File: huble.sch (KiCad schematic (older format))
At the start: 32 parts, among them J7 USB_C_Receptacle, J8 USB_C_Receptacle, P1 CONN_01X04, P2 CONN_02X03, Q1 Q_PMOS_GSD, Q2 Q_PMOS_GSD, U3 rgbled, U4 ATmega32U4, U5 24LC16, Y2 Crystal_GND24

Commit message: fixed missing cap on schematic, and fixed up post move netlist
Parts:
- C9: footprint Capacitors_Tantalum_SMD:TantalC_SizeA_EIA-3216_Wave -> Capacitors_Tantalum_SMD:CP_Tantalum_Case-A_EIA-3216-18_Reflow
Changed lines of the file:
@@
 $Descr A4 11693 8268
 encoding utf-8
-Sheet 2 3
+Sheet 2 2
 Title "Huble"
 Date "2017-08-16"
@@
 F 0 "C9" H 5768 1346 50  0000 L CNN
 F 1 "47u 6.3v" H 5768 1255 50  0000 L CNN
-F 2 "Capacitors_Tantalum_SMD:TantalC_SizeA_EIA-3216_Wave" H 5688 1150 50  0001 C CNN
+F 2 "Capacitors_Tantalum_SMD:CP_Tantalum_Case-A_EIA-3216-18_Reflow" H 5688 1150 50  0001 C CNN
 F 3 "" H 5650 1300 50  0000 C CNN
 F 4 "1432351" H 5650 1300 60  0001 C CNN "farnell #"
@@
 $EndComp
 $Comp
-L +5C #PWR?
+L +5C #PWR053
 U 1 1 5A6A530B
 P 2050 750
-F 0 "#PWR?" H 2050 600 50  0001 C CNN
+F 0 "#PWR053" H 2050 600 50  0001 C CNN
 F 1 "+5C" H 2065 923 50  0000 C CNN
 F 2 "" H 2050 750 50  0001 C CNN
@@
 $EndComp
 $Comp
-L +5C #PWR?
+L +5C #PWR054
 U 1 1 5A6A53AB
 P 2150 4200
-F 0 "#PWR?" H 2150 4050 50  0001 C CNN
+F 0 "#PWR054" H 2150 4050 50  0001 C CNN
 F 1 "+5C" H 2165 4373 50  0000 C CNN
 F 2 "" H 2150 4200 50  0001 C CNN

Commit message: remove wrong farnell codes, use same 47u tant cap in both places
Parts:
- J7, J8: farnell # 2564554 -> 2524075
- R14, R15, R16: farnell # 2447609 -> (none)
- Y2: value Crystal_GND24 -> 16mhz
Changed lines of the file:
@@
 F 2 "Resistors_SMD:R_0805" V 8480 5400 30  0001 C CNN
 F 3 "" H 8550 5400 30  0000 C CNN
-F 4 "2447609" H 8550 5400 60  0001 C CNN "farnell #"
 	1    8550 5400
 	0    1    1    0
@@
 F 2 "Resistors_SMD:R_0805" V 8480 5700 30  0001 C CNN
 F 3 "" H 8550 5700 30  0000 C CNN
-F 4 "2447609" H 8550 5700 60  0001 C CNN "farnell #"
 	1    8550 5700
 	0    1    1    0
@@
 F 2 "Resistors_SMD:R_0805" V 8480 6000 30  0001 C CNN
 F 3 "" H 8550 6000 30  0000 C CNN
-F 4 "2447609" H 8550 6000 60  0001 C CNN "farnell #"
 	1    8550 6000
 	0    1    1    0
@@
 F 2 "fp:usb-c-24smt" H 1350 2350 50  0001 C CNN
 F 3 "http://www.usb.org/developers/docs/usb_31_033017.zip" H 1350 2350 50  0001 C CNN
-F 4 "2564554" H 1200 2350 60  0001 C CNN "farnell #"
+F 4 "2524075" H 1200 2350 60  0001 C CNN "farnell #"
 	1    1200 2350
 	1    0    0    -1
@@
 P 7300 3800
 F 0 "Y2" V 7254 4041 50  0000 L CNN
-F 1 "Crystal_GND24" V 7345 4041 50  0000 L CNN
+F 1 "16mhz" V 7345 4041 50  0000 L CNN
 F 2 "Crystals:Crystal_SMD_3225-4pin_3.2x2.5mm" H 7300 3800 50  0001 C CNN
 F 3 "" H 7300 3800 50  0001 C CNN
@@
 F 2 "fp:usb-c-24smt" H 1400 5750 50  0001 C CNN
 F 3 "http://www.usb.org/developers/docs/usb_31_033017.zip" H 1400 5750 50  0001 C CNN
-F 4 "2564554" H 1250 5750 60  0001 C CNN "farnell #"
+F 4 "2524075" H 1250 5750 60  0001 C CNN "farnell #"
 	1    1250 5750
 	1    0    0    -1

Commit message: updated for BOM
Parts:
- removed C12, C13: 20pf, Capacitors_SMD:C_0805, symbol C
- removed U5: 24LC16, Housings_SOIC:SOIC-8_3.9x4.9mm_Pitch1.27mm, symbol 24LC16
- removed Y2: 16mhz, Crystals:Crystal_SMD_3225-4pin_3.2x2.5mm, symbol Crystal_GND24
- added R20, R22, R23: 60R, 125mW, 5%, Resistors_SMD:R_0805, symbol R
- added R21: 100R, 125mW, 5%, Resistors_SMD:R_0805, symbol R
- added U5, U6: 4 pin RGB led, com anode, red: 500mcd 620nm. Gree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, fp:3528-4p, symbol rgbled
- C10: value 4.7u -> 4.7uF, ceramic, 6v, 10%, x5r; supplier (none) -> any/open
- C11: value 0.1u -> 0.1uF, ceramic, 6v, 10%, x5r; supplier (none) -> any/open
- C14: value 1u -> 1uF, ceramic, 6v, 10%, x5r; supplier (none) -> any/open
- C9: value 47u 6.3v -> 47uF, 6.3v, 10%, tantalum; supplier (none) -> AVX; supplier PN (none) -> TAJC476K006RNJ
- J7, J8: value USB_C_Receptacle -> USB C type 2.0 SMT 16pin; farnell # 2524075 -> (none); supplier (none) -> contact technology corp; supplier PN (none) -> sbc-160s-202-s338
- P1, P2, TP11, TP3, W1, W2: supplier (none) -> dnp
- Q1, Q2: value Q_PMOS_GSD -> PMOS, -3.6A, 0.02R; supplier (none) -> diodes inc; supplier PN (none) -> DMP2035U
- R10, R9: value 4.7k -> 4.7k, 125mW, 5%; supplier (none) -> any/open
- R11: value 10k -> 10k, 125mW, 5%; farnell # 2447553 -> (none); supplier (none) -> any/open
- R12: value 22r -> 100R, 125mW, 5%; farnell # 2447609 -> (none); supplier (none) -> any/open
- R13: value 22r -> 60R, 125mW, 5%; farnell # 2447609 -> (none); supplier (none) -> any/open
- R14: value 100R -> 100R, 125mW, 5%; supplier (none) -> any/open
- R15, R16: value 60R -> 60R, 125mW, 5%; supplier (none) -> any/open
- R18, R19: value 10k -> 10k, 125mW, 5%; farnell # 2073784 -> (none); supplier (none) -> any/open
- R7, R8: farnell # 9333681 -> (none); supplier (none) -> dnp
- U3: value rgbled -> 4 pin RGB led, com anode, red: 500mcd 620nm. Green: 1000mcd 520nm. Blue: 500mcd 460nm.; supplier (none) -> any/open
- U4: value ATmega32U4 -> atmel samd21g; farnell # 2425127 -> (none); supplier (none) -> microchip; supplier PN (none) -> ATSAMD21G18A-MU
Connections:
- wire segments 54 -> 49
- no-connect marks 41 -> 40
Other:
- note added: "can't use the same power flag on both lines, or they get connected together!"
- note added: "will need level conversion if switching to 3.3v arm"
- note removed: "1579573"
- note removed: "256kbit eeprom for extra layers"
- note removed: "load cap is 20pf. assume stray cap is 5pf, so use 30pf caps"

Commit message: v2.1 ready for fab
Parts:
- removed C9: 47uF, 6.3v, 10%, tantalum, Capacitors_Tantalum_SMD:CP_Tantalum_Case-A_EIA-3216-18_Reflow, symbol CP
- removed J7, J8: USB C type 2.0 SMT 16pin, fp:usb-c-24smt, symbol USB_C_Receptacle
- removed P1: CONN_01X04, Pin_Headers:Pin_Header_Straight_1x04_Pitch2.54mm, symbol Conn_01x04
- removed Q1, Q2: PMOS, -3.6A, 0.02R, TO_SOT_Packages_SMD:SOT-23, symbol Q_PMOS_GSD
- removed R11, R18, R19: 10k, 125mW, 5%, Resistors_SMD:R_0805, symbol R
- removed TP11: TEST, Measurement_Points:Measurement_Point_Round-SMD-Pad_Small, symbol TEST
- removed U4: atmel samd21g, Housings_DFN_QFN:QFN-44-1EP_7x7mm_Pitch0.5mm, symbol ATmega32U4-RESCUE-huble
- removed W1, W2: TEST_1P, Measurement_Points:Measurement_Point_Round-SMD-Pad_Small, symbol TEST_1P
- added C12, C13, C9: 0.1uF, ceramic, 6v, 10%, x5r, Capacitors_SMD:C_0603, symbol C
- added C16: 20pf, ceramic, 6v, 5%, Capacitors_SMD:C_0603, symbol C
- added J2, J3: USB_C_Receptacle_16pin, fp:usb-c-16smt, symbol USB_C_Receptacle_16pin
- added Q1, Q2, Q3, Q4: Q_NMOS_GSD, TO_SOT_Packages_SMD:SOT-323_SC-70, symbol Q_NMOS_GSD
- added TP1, TP2, TP4: TEST, Measurement_Points:Measurement_Point_Round-SMD-Pad_Small, symbol TEST
- added U4: samd21j, Housings_DFN_QFN:QFN-64-1EP_9x9mm_Pitch0.5mm, symbol samd21j
- added U7: MMBZx, TO_SOT_Packages_SMD:SOT-23, symbol MMBZx
- added Y2: 32.768khz, Crystals:Crystal_SMD_3215-2pin_3.2x1.5mm, symbol Crystal
- C10: value 4.7uF, ceramic, 6v, 10%, x5r -> 10uF, ceramic, 6v, 10%, x5r; footprint Capacitors_SMD:C_0805 -> Capacitors_SMD:C_0603; MOQ (none) -> Value; leadtime (none) -> Value; supplier PN (none) -> Value
- C11: footprint Capacitors_SMD:C_0805 -> Capacitors_SMD:C_0603; MOQ (none) -> Value; leadtime (none) -> Value; supplier PN (none) -> Value
- C14: value 1uF, ceramic, 6v, 10%, x5r -> 20pf, ceramic, 6v, 5%; footprint Capacitors_SMD:C_0805 -> Capacitors_SMD:C_0603; farnell # 1759422 -> 2581087
- R10, R9: value 4.7k, 125mW, 5% -> 10k, 125mW, 5%; footprint Resistors_SMD:R_0805 -> Resistors_SMD:R_0603
- R12, R13, R14, R15, R16, R20, R21, R22, R23: footprint Resistors_SMD:R_0805 -> Resistors_SMD:R_0603
- R7, R8: value 0R -> 10k, 125mW, 5%; footprint Resistors_SMD:R_0805 -> Resistors_SMD:R_0603; farnell # (none) -> 2073784; supplier dnp -> any/open
- TP3: supplier dnp -> (none)
- U3, U5, U6: MOQ (none) -> Value; leadtime (none) -> Value; supplier PN (none) -> Value
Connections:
- net labels added: +3.3V, dfp-l-cc, dfp-r-cc, gclk_io_0, left-usb-gnd, pwm1_b, pwm1_g, pwm1_r, pwm2_b, pwm2_g, pwm2_r, pwm3_b, pwm3_g, pwm3_r, right-usb-gnd, scl5, sda5, swclk, swdio, ufp-cc
- net labels removed: +5C, miso, mosi, pwm_b, pwm_g, pwm_r, sck, usbc-dn, usbc-dp
- wire segments 49 -> 53
- no-connect marks 40 -> 32
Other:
- note added: "esd protection"
- note added: "https://www.nxp.com/docs/en/application-note/AN10441.pdf"
- note added: "level translate\n"
- note removed: "can't use the same power flag on both lines, or they get connected together!"
- note removed: "will need level conversion if switching to 3.3v arm"
- moved on the sheet: P2, R10, R12, R13, R14, R15, R16, R20, R21, R22, R23, R9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

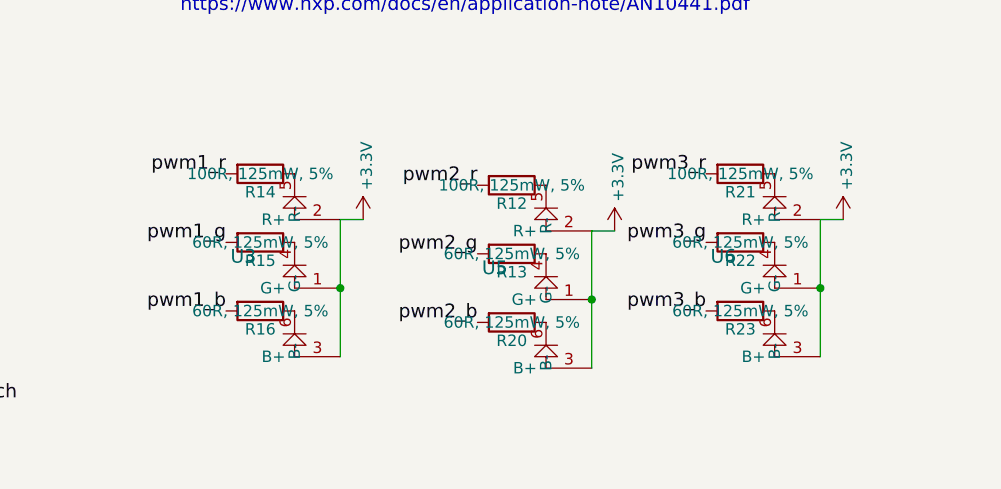
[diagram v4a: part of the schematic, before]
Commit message: bom updated for 0603 parts and farnell order
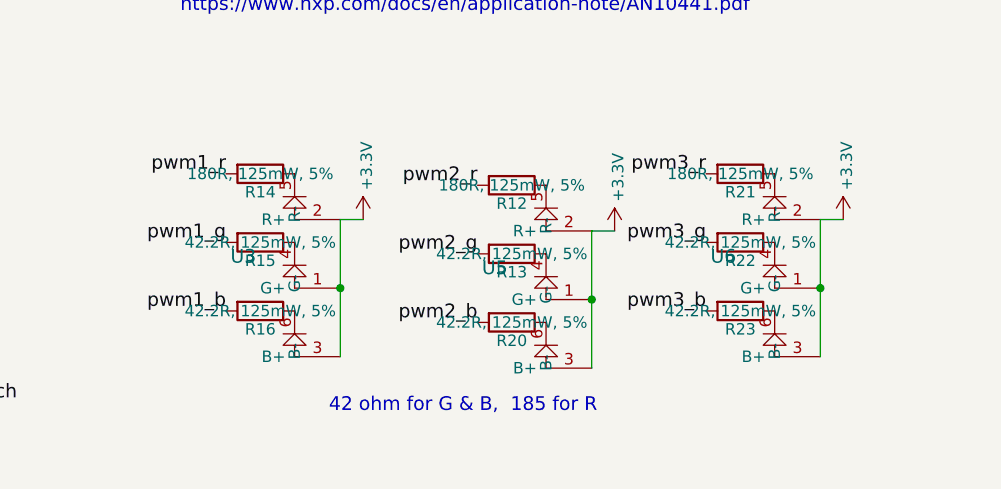
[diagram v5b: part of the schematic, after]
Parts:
- C10: farnell # 1709210 -> 1288201
- C11, C12, C13, C9: farnell # 1759167 -> 2522395
- C14, C16: farnell # 2581087 -> 1865475
- R10, R7, R8, R9: farnell # 2073784 -> 2447230
- R12, R14, R21: value 100R, 125mW, 5% -> 180R, 125mW, 5%; farnell # (none) -> 2447267
- R13, R15, R16, R20, R22, R23: value 60R, 125mW, 5% -> 42.2R, 125mW, 5%; farnell # (none) -> 2694864
- TP1, TP2, TP3, TP4, U3, U5, U6: farnell # (none) -> dnp
- U4: MOQ (none) -> Value; farnell # (none) -> 2409254; leadtime (none) -> Value; supplier (none) -> Microchip; supplier PN (none) -> ATSAMD21J18A-MU
- U7: farnell # 2317793 -> 1431253
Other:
- note added: "42 ohm for G & B, 185 for R"
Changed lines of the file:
@@
 F 2 "Capacitors_SMD:C_0603" H 6038 1150 30  0001 C CNN
 F 3 "" H 6000 1300 60  0000 C CNN
-F 4 "1709210" H 6000 1300 60  0001 C CNN "farnell #"
+F 4 "1288201" H 6000 1300 60  0001 C CNN "farnell #"
 F 5 "any/open" H 0   0   60  0001 C CNN "supplier"
 F 6 "Value" H 6000 1300 60  0001 C CNN "supplier PN"
@@
 F 2 "Resistors_SMD:R_0603" V 5380 4850 30  0001 C CNN
 F 3 "" H 5450 4850 30  0000 C CNN
-F 4 "2073784" H 5450 4850 60  0001 C CNN "farnell #"
+F 4 "2447230" H 5450 4850 60  0001 C CNN "farnell #"
 F 5 "any/open" H 950 1650 60  0001 C CNN "supplier"
 	1    5450 4850
@@
 F 2 "Resistors_SMD:R_0603" V 5580 5100 30  0001 C CNN
 F 3 "" H 5650 5100 30  0000 C CNN
-F 4 "2073784" H 5650 5100 60  0001 C CNN "farnell #"
+F 4 "2447230" H 5650 5100 60  0001 C CNN "farnell #"
 F 5 "any/open" H 1150 1600 60  0001 C CNN "supplier"
 	1    5650 5100
@@
 F 6 "Value" H 4100 6850 60  0001 C CNN "MOQ"
 F 7 "Value" H 4100 6850 60  0001 C CNN "leadtime"
+F 8 "dnp" H 0   0   60  0001 C CNN "farnell #"
 	1    4100 6850
 	1    0    0    -1
@@
 P 3950 6350
 F 0 "R14" V 4030 6350 50  0000 C CNN
-F 1 "100R, 125mW, 5%" V 3950 6350 50  0000 C CNN
+F 1 "180R, 125mW, 5%" V 3950 6350 50  0000 C CNN
 F 2 "Resistors_SMD:R_0603" V 3880 6350 30  0001 C CNN
 F 3 "" H 3950 6350 30  0000 C CNN
 F 4 "any/open" H -4600 950 60  0001 C CNN "supplier"
+F 5 "2447267" H 0   0   60  0001 C CNN "farnell #"
 	1    3950 6350
 	0    1    1    0
@@
 P 3950 6650
 F 0 "R15" V 4030 6650 50  0000 C CNN
-F 1 "60R, 125mW, 5%" V 3950 6650 50  0000 C CNN
+F 1 "42.2R, 125mW, 5%" V 3950 6650 50  0000 C CNN
 F 2 "Resistors_SMD:R_0603" V 3880 6650 30  0001 C CNN
 F 3 "" H 3950 6650 30  0000 C CNN
 F 4 "any/open" H -4600 950 60  0001 C CNN "supplier"
+F 5 "2694864" H 0   0   60  0001 C CNN "farnell #"
 	1    3950 6650
 	0    1    1    0
@@
 P 3950 6950
 F 0 "R16" V 4030 6950 50  0000 C CNN
-F 1 "60R, 125mW, 5%" V 3950 6950 50  0000 C CNN
+F 1 "42.2R, 125mW, 5%" V 3950 6950 50  0000 C CNN
 F 2 "Resistors_SMD:R_0603" V 3880 6950 30  0001 C CNN
 F 3 "" H 3950 6950 30  0000 C CNN
 F 4 "any/open" H -4600 950 60  0001 C CNN "supplier"
+F 5 "2694864" H 0   0   60  0001 C CNN "farnell #"
 	1    3950 6950
 	0    1    1    0
@@
 F 6 "Value" H 5200 6900 60  0001 C CNN "MOQ"
 F 7 "Value" H 5200 6900 60  0001 C CNN "leadtime"
+F 8 "dnp" H 0   0   60  0001 C CNN "farnell #"
 	1    5200 6900
 	1    0    0    -1
@@
 P 5050 6400
 F 0 "R12" V 5130 6400 50  0000 C CNN
-F 1 "100R, 125mW, 5%" V 5050 6400 50  0000 C CNN
+F 1 "180R, 125mW, 5%" V 5050 6400 50  0000 C CNN
 F 2 "Resistors_SMD:R_0603" V 4980 6400 30  0001 C CNN
 F 3 "" H 5050 6400 30  0000 C CNN
 F 4 "any/open" H -4600 950 60  0001 C CNN "supplier"
+F 5 "2447267" H 0   0   60  0001 C CNN "farnell #"
 	1    5050 6400
 	0    1    1    0
@@
 P 5050 6700
 F 0 "R13" V 5130 6700 50  0000 C CNN
-F 1 "60R, 125mW, 5%" V 5050 6700 50  0000 C CNN
+F 1 "42.2R, 125mW, 5%" V 5050 6700 50  0000 C CNN
 F 2 "Resistors_SMD:R_0603" V 4980 6700 30  0001 C CNN
 F 3 "" H 5050 6700 30  0000 C CNN
 F 4 "any/open" H -4600 950 60  0001 C CNN "supplier"
+F 5 "2694864" H 0   0   60  0001 C CNN "farnell #"
 	1    5050 6700
 	0    1    1    0
@@
 P 5050 7000
 F 0 "R20" V 5130 7000 50  0000 C CNN
-F 1 "60R, 125mW, 5%" V 5050 7000 50  0000 C CNN
+F 1 "42.2R, 125mW, 5%" V 5050 7000 50  0000 C CNN
 F 2 "Resistors_SMD:R_0603" V 4980 7000 30  0001 C CNN
 F 3 "" H 5050 7000 30  0000 C CNN
 F 4 "any/open" H -4600 950 60  0001 C CNN "supplier"
+F 5 "2694864" H 0   0   60  0001 C CNN "farnell #"
 	1    5050 7000
 	0    1    1    0
@@
 F 6 "Value" H 6200 6850 60  0001 C CNN "MOQ"
 F 7 "Value" H 6200 6850 60  0001 C CNN "leadtime"
+F 8 "dnp" H 0   0   60  0001 C CNN "farnell #"
 	1    6200 6850
 	1    0    0    -1
@@
 P 6050 6350
 F 0 "R21" V 6130 6350 50  0000 C CNN
-F 1 "100R, 125mW, 5%" V 6050 6350 50  0000 C CNN
+F 1 "180R, 125mW, 5%" V 6050 6350 50  0000 C CNN
 F 2 "Resistors_SMD:R_0603" V 5980 6350 30  0001 C CNN
 F 3 "" H 6050 6350 30  0000 C CNN
 F 4 "any/open" H -4600 950 60  0001 C CNN "supplier"
+F 5 "2447267" H 0   0   60  0001 C CNN "farnell #"
 	1    6050 6350
 	0    1    1    0
@@
 P 6050 6650
 F 0 "R22" V 6130 6650 50  0000 C CNN
-F 1 "60R, 125mW, 5%" V 6050 6650 50  0000 C CNN
+F 1 "42.2R, 125mW, 5%" V 6050 6650 50  0000 C CNN
 F 2 "Resistors_SMD:R_0603" V 5980 6650 30  0001 C CNN
 F 3 "" H 6050 6650 30  0000 C CNN
 F 4 "any/open" H -4600 950 60  0001 C CNN "supplier"
+F 5 "2694864" H 0   0   60  0001 C CNN "farnell #"
 	1    6050 6650
 	0    1    1    0
@@
 P 6050 6950
 F 0 "R23" V 6130 6950 50  0000 C CNN
-F 1 "60R, 125mW, 5%" V 6050 6950 50  0000 C CNN
+F 1 "42.2R, 125mW, 5%" V 6050 6950 50  0000 C CNN
 F 2 "Resistors_SMD:R_0603" V 5980 6950 30  0001 C CNN
 F 3 "" H 6050 6950 30  0000 C CNN
 F 4 "any/open" H -4600 950 60  0001 C CNN "supplier"
+F 5 "2694864" H 0   0   60  0001 C CNN "farnell #"
 	1    6050 6950
 	0    1    1    0
@@
 F 2 "Housings_DFN_QFN:QFN-64-1EP_9x9mm_Pitch0.5mm" H 8400 3300 60  0001 C CNN
 F 3 "" H 8400 3300 60  0001 C CNN
+F 4 "2409254" H 8400 3300 60  0001 C CNN "farnell #"
+F 5 "Microchip" H 8400 3300 60  0001 C CNN "supplier"
+F 6 "ATSAMD21J18A-MU " H 8400 3300 60  0001 C CNN "supplier PN"
+F 7 "Value" H 8400 3300 60  0001 C CNN "MOQ"
+F 8 "Value" H 8400 3300 60  0001 C CNN "leadtime"
 	1    8400 3300
 	1    0    0    -1
@@
 F 2 "Capacitors_SMD:C_0603" H 5688 1150 30  0001 C CNN
 F 3 "" H 5650 1300 60  0000 C CNN
-F 4 "1759167" H 5650 1300 60  0001 C CNN "farnell #"
+F 4 "2522395" H 5650 1300 60  0001 C CNN "farnell #"
 F 5 "any/open" H -700 0   60  0001 C CNN "supplier"
 F 6 "Value" H 5650 1300 60  0001 C CNN "supplier PN"
@@
 F 2 "Capacitors_SMD:C_0603" H 5388 1150 30  0001 C CNN
 F 3 "" H 5350 1300 60  0000 C CNN
-F 4 "1759167" H 5350 1300 60  0001 C CNN "farnell #"
+F 4 "2522395" H 5350 1300 60  0001 C CNN "farnell #"
 F 5 "any/open" H -1000 0   60  0001 C CNN "supplier"
 F 6 "Value" H 5350 1300 60  0001 C CNN "supplier PN"
@@
 F 2 "Capacitors_SMD:C_0603" H 5088 1150 30  0001 C CNN
 F 3 "" H 5050 1300 60  0000 C CNN
-F 4 "1759167" H 5050 1300 60  0001 C CNN "farnell #"
+F 4 "2522395" H 5050 1300 60  0001 C CNN "farnell #"
 F 5 "any/open" H -1300 0   60  0001 C CNN "supplier"
 F 6 "Value" H 5050 1300 60  0001 C CNN "supplier PN"
@@
 F 2 "Capacitors_SMD:C_0603" H 4788 1150 30  0001 C CNN
 F 3 "" H 4750 1300 60  0000 C CNN
-F 4 "1759167" H 4750 1300 60  0001 C CNN "farnell #"
+F 4 "2522395" H 4750 1300 60  0001 C CNN "farnell #"
 F 5 "any/open" H -1600 0   60  0001 C CNN "supplier"
 F 6 "Value" H 4750 1300 60  0001 C CNN "supplier PN"
@@
 F 2 "Capacitors_SMD:C_0603" H 5688 2650 50  0001 C CNN
 F 3 "" H 5650 2800 50  0001 C CNN
-F 4 "2581087" H 5650 2800 60  0001 C CNN "farnell #"
+F 4 "1865475" H 5650 2800 60  0001 C CNN "farnell #"
 F 5 "any/open" H 4200 -2500 60  0001 C CNN "supplier"
 	1    5650 2800
@@
 F 2 "Capacitors_SMD:C_0603" H 5688 2050 50  0001 C CNN
 F 3 "" H 5650 2200 50  0001 C CNN
-F 4 "2581087" H 5650 2200 60  0001 C CNN "farnell #"
+F 4 "1865475" H 5650 2200 60  0001 C CNN "farnell #"
 F 5 "any/open" H 4200 -2500 60  0001 C CNN "supplier"
 	1    5650 2200
@@
 F 2 "Resistors_SMD:R_0603" V 4080 4850 30  0001 C CNN
 F 3 "" H 4150 4850 30  0000 C CNN
-F 4 "2073784" H 4150 4850 60  0001 C CNN "farnell #"
+F 4 "2447230" H 4150 4850 60  0001 C CNN "farnell #"
 F 5 "any/open" H -350 1350 60  0001 C CNN "supplier"
 	1    4150 4850
@@
 F 2 "Resistors_SMD:R_0603" V 3880 5100 30  0001 C CNN
 F 3 "" H 3950 5100 30  0000 C CNN
-F 4 "2073784" H 3950 5100 60  0001 C CNN "farnell #"
+F 4 "2447230" H 3950 5100 60  0001 C CNN "farnell #"
 F 5 "any/open" H -550 1600 60  0001 C CNN "supplier"
 	1    3950 5100
@@
 F 2 "TO_SOT_Packages_SMD:SOT-23" H 5200 3700 60  0001 C CNN
 F 3 "" H 5200 3700 60  0001 C CNN
-F 4 "2317793" H 5200 3700 60  0001 C CNN "farnell #"
+F 4 "1431253" H 5200 3700 60  0001 C CNN "farnell #"
 F 5 "Value" H 5200 3700 60  0001 C CNN "supplier"
 F 6 "Value" H 5200 3700 60  0001 C CNN "supplier PN"
@@
 F 2 "Measurement_Points:Measurement_Point_Round-SMD-Pad_Small" H 7300 2850 50  0001 C CNN
 F 3 "" H 7300 2850 50  0001 C CNN
+F 4 "dnp" H 0   0   60  0001 C CNN "farnell #"
 	1    7300 2850
 	0    -1   -1   0
@@
 F 2 "Measurement_Points:Measurement_Point_Round-SMD-Pad_Small" H 7300 2950 50  0001 C CNN
 F 3 "" H 7300 2950 50  0001 C CNN
+F 4 "dnp" H 0   0   60  0001 C CNN "farnell #"
 	1    7300 2950
 	0    -1   -1   0
@@
 F 2 "Measurement_Points:Measurement_Point_Round-SMD-Pad_Small" H 7300 3050 50  0001 C CNN
 F 3 "" H 7300 3050 50  0001 C CNN
+F 4 "dnp" H 0   0   60  0001 C CNN "farnell #"
 	1    7300 3050
 	0    -1   -1   0
@@
 F 2 "Measurement_Points:Measurement_Point_Round-SMD-Pad_Small" H 7300 3150 50  0001 C CNN
 F 3 "" H 7300 3150 50  0001 C CNN
+F 4 "dnp" H 0   0   60  0001 C CNN "farnell #"
 	1    7300 3150
 	0    -1   -1   0
@@
 Text Label 2150 3800 0    60   ~ 0
 left-usb-gnd
+Text Notes 4250 7400 0    60   ~ 0
+42 ohm for G & B,  185 for R
 $EndSCHEMATC

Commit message: fixed vddcore error
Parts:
- removed C13: 0.1uF, ceramic, 6v, 10%, x5r, Capacitors_SMD:C_0603, symbol C
- added C?: 1uF, ceramic, 6v, 10%, x5r, Capacitors_SMD:C_0603, symbol C
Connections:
- net labels added: samd-usb-n, samd-usb-p
- net labels removed: atmega-usb-n, atmega-usb-p
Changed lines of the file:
@@
 $EndComp
 Text GLabel 10050 2850 2    60   Input ~ 0
-atmega-usb-p
+samd-usb-p
 Text GLabel 10050 2950 2    60   Input ~ 0
-atmega-usb-n
+samd-usb-n
 NoConn ~ 1800 3550
 NoConn ~ 1800 3650
@@
 $EndComp
 $Comp
-L +3.3V #PWR047
-U 1 1 5A9D9CDD
-P 8600 2000
-F 0 "#PWR047" H 8600 1850 50  0001 C CNN
-F 1 "+3.3V" V 8615 2128 50  0000 L CNN
-F 2 "" H 8600 2000 50  0001 C CNN
-F 3 "" H 8600 2000 50  0001 C CNN
-	1    8600 2000
-	1    0    0    -1
-$EndComp
-$Comp
 L Earth #PWR048
 U 1 1 5A9D9E4B
@@
 F 3 "" H 8100 4800 50  0001 C CNN
 	1    8100 4800
-	-1   0    0    1
-$EndComp
-$Comp
-L C C13
-U 1 1 5A9DAA08
-P 5650 1300
-F 0 "C13" H 5675 1400 50  0000 L CNN
-F 1 "0.1uF, ceramic, 6v, 10%, x5r" H 5675 1200 50  0001 L CNN
-F 2 "Capacitors_SMD:C_0603" H 5688 1150 30  0001 C CNN
-F 3 "" H 5650 1300 60  0000 C CNN
-F 4 "2522395" H 5650 1300 60  0001 C CNN "farnell #"
-F 5 "any/open" H -700 0   60  0001 C CNN "supplier"
-F 6 "Value" H 5650 1300 60  0001 C CNN "supplier PN"
-F 7 "Value" H 5650 1300 60  0001 C CNN "MOQ"
-F 8 "Value" H 5650 1300 60  0001 C CNN "leadtime"
-	1    5650 1300
 	-1   0    0    1
 $EndComp
@@
 	8500 2000 8500 2200
 Wire Wire Line
-	8600 2000 8600 2200
+	8600 1450 8600 2200
 Wire Wire Line
 	8700 1900 8700 2200
@@
 Text Notes 4250 7400 0    60   ~ 0
 42 ohm for G & B,  185 for R
+$Comp
+L Earth #PWR023
+U 1 1 5AB4F868
+P 8600 1150
+F 0 "#PWR023" H 8600 900 50  0001 C CNN
+F 1 "Earth" H 8600 1000 50  0001 C CNN
+F 2 "" H 8600 1150 60  0000 C CNN
+F 3 "" H 8600 1150 60  0000 C CNN
+	1    8600 1150
+	-1   0    0    1
+$EndComp
+$Comp
+L C C?
+U 1 1 5AB50123
+P 8600 1300
+F 0 "C?" H 8715 1346 50  0000 L CNN
+F 1 "1uF, ceramic, 6v, 10%, x5r" H 8715 1255 50  0000 L CNN
+F 2 "Capacitors_SMD:C_0603" H 8638 1150 50  0001 C CNN
+F 3 "" H 8600 1300 50  0001 C CNN
+F 4 "any/open" H 7150 -1350 60  0001 C CNN "supplier"
+F 5 "1865556" H 7150 -1350 60  0001 C CNN "farnell #"
+	1    8600 1300
+	1    0    0    -1
+$EndComp
 $EndSCHEMATC
